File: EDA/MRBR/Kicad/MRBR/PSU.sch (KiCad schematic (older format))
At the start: 3 parts, among them U2 NCP1117ST33T3G

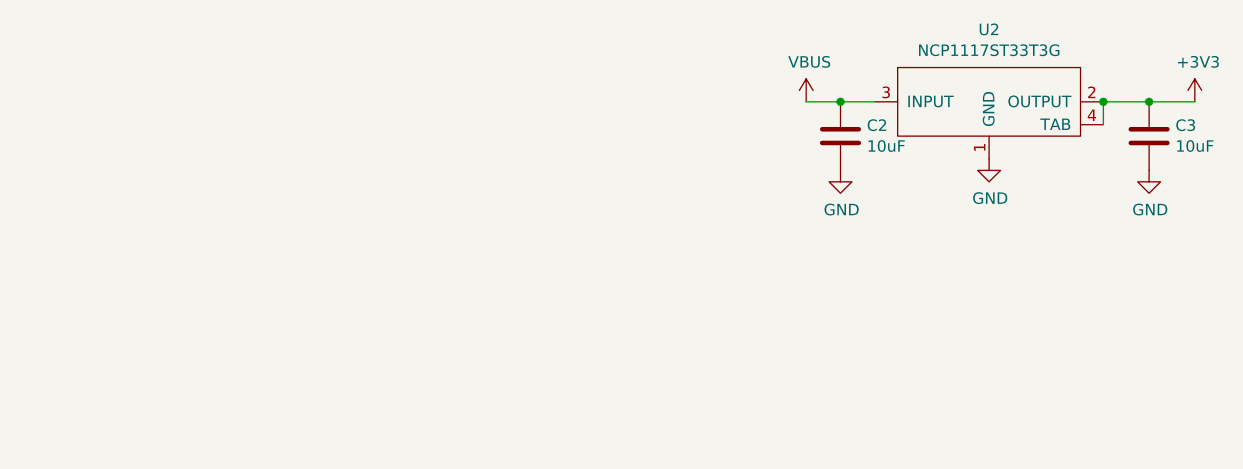
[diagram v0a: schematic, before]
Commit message: Added barrel jack to PSU
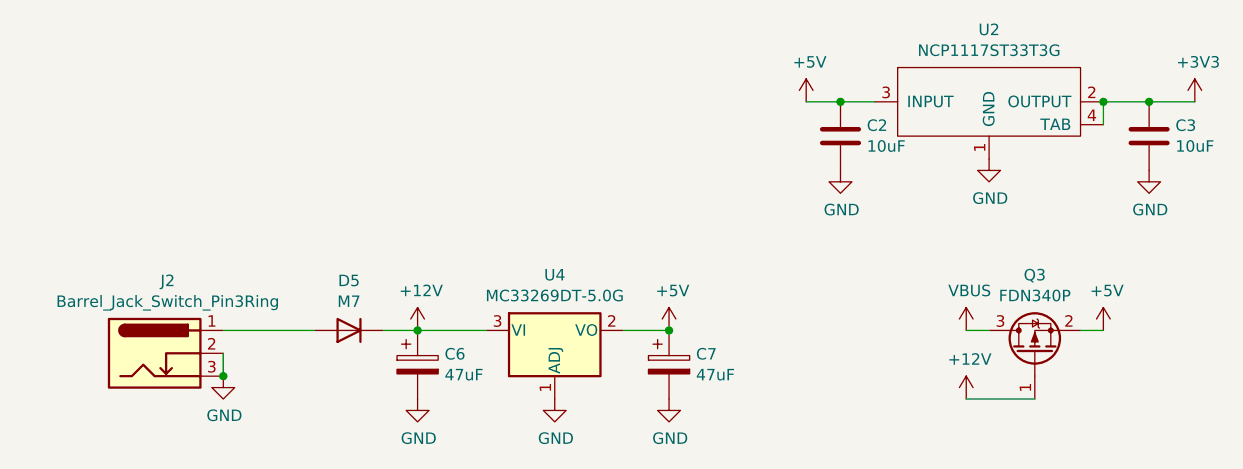
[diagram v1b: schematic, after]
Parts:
- added C6, C7: 47uF, Capacitor_SMD:CP_Elec_6.3x7.7, symbol Device:CP
- added D5: M7, Diode_SMD:D_SMA, symbol Device:D
- added J2: Barrel_Jack_Switch_Pin3Ring, Connector_BarrelJack:BarrelJack_Wuerth_6941xx301002, symbol Connector:Barrel_Jack_Switch_Pin3Ring
- added Q3: FDN340P, Package_TO_SOT_SMD:SOT-23, symbol Transistor_FET:FDN340P
- added U4: MC33269DT-5.0G, Package_TO_SOT_SMD:TO-252-2, symbol Regulator_Linear:MC33269DT-5.0G
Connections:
- net GND: now also C6.2, C7.2, J2.2, J2.3, U4.1 (ADJ)
- net VBUS: now also Q3.3 (D); no longer C2.1, U2.3 (INPUT)
- new net: D5.2 (A), J2.1
- new net +12V: C6.1, D5.1 (K), Q3.1 (G), U4.3 (VI)
- new net +5V: C2.1, C7.1, Q3.2 (S), U2.3 (INPUT), U4.2 (VO)
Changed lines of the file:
@@
-$EndComp
-$Comp
-L power:VBUS #PWR06
-U 1 1 611D0F4B
-P 4750 2750
-F 0 "#PWR06" H 4750 2600 50  0001 C CNN
-F 1 "VBUS" H 4765 2923 50  0000 C CNN
-F 2 "" H 4750 2750 50  0001 C CNN
-F 3 "" H 4750 2750 50  0001 C CNN
-	1    4750 2750
-	1    0    0    -1
 $EndComp
 $Comp
@@
 Wire Wire Line
 	6250 2750 6450 2750
+$Comp
+L Connector:Barrel_Jack_Switch_Pin3Ring J2
+U 1 1 612526B4
+P 1900 3850
+F 0 "J2" H 1957 4167 50  0000 C CNN
+F 1 "Barrel_Jack_Switch_Pin3Ring" H 1957 4076 50  0000 C CNN
+F 2 "Connector_BarrelJack:BarrelJack_Wuerth_6941xx301002" H 1950 3810 50  0001 C CNN
+F 3 "~" H 1950 3810 50  0001 C CNN
+	1    1900 3850
+	1    0    0    -1
+$EndComp
+$Comp
+L Device:D D5
+U 1 1 612543C2
+P 2750 3750
+F 0 "D5" H 2750 3533 50  0000 C CNN
+F 1 "M7" H 2750 3624 50  0000 C CNN
+F 2 "Diode_SMD:D_SMA" H 2750 3750 50  0001 C CNN
+F 3 "~" H 2750 3750 50  0001 C CNN
+	1    2750 3750
+	-1   0    0    1
+$EndComp
+Wire Wire Line
+	2200 3750 2600 3750
+Wire Wire Line
+	2200 3850 2200 3950
+$Comp
+L power:GND #PWR020
+U 1 1 612552FD
+P 2200 3950
+F 0 "#PWR020" H 2200 3700 50  0001 C CNN
+F 1 "GND" H 2205 3777 50  0000 C CNN
+F 2 "" H 2200 3950 50  0001 C CNN
+F 3 "" H 2200 3950 50  0001 C CNN
+	1    2200 3950
+	1    0    0    -1
+$EndComp
+Connection ~ 2200 3950
+$Comp
+L Device:CP C6
+U 1 1 61255DE4
+P 3050 3900
+F 0 "C6" H 3168 3946 50  0000 L CNN
+F 1 "47uF" H 3168 3855 50  0000 L CNN
+F 2 "Capacitor_SMD:CP_Elec_6.3x7.7" H 3088 3750 50  0001 C CNN
+F 3 "~" H 3050 3900 50  0001 C CNN
+	1    3050 3900
+	1    0    0    -1
+$EndComp
+$Comp
+L Device:CP C7
+U 1 1 61257275
+P 4150 3900
+F 0 "C7" H 4268 3946 50  0000 L CNN
+F 1 "47uF" H 4268 3855 50  0000 L CNN
+F 2 "Capacitor_SMD:CP_Elec_6.3x7.7" H 4188 3750 50  0001 C CNN
+F 3 "~" H 4150 3900 50  0001 C CNN
+	1    4150 3900
+	1    0    0    -1
+$EndComp
+$Comp
+L Regulator_Linear:MC33269DT-5.0G U4
+U 1 1 6125C1E8
+P 3650 3750
+F 0 "U4" H 3650 3992 50  0000 C CNN
+F 1 "MC33269DT-5.0G" H 3650 3901 50  0000 C CNN
+F 2 "Package_TO_SOT_SMD:TO-252-2" H 3650 4000 50  0001 C CIN
+F 3 "https://datasheet.lcsc.com/lcsc/1811141628_ON-Semiconductor-MC33269DT-5-0G_C232420.pdf" H 3650 3750 50  0001 C CNN
+	1    3650 3750
+	1    0    0    -1
+$EndComp
+Wire Wire Line
+	2900 3750 3050 3750
+Connection ~ 3050 3750
+Wire Wire Line
+	3050 3750 3350 3750
+$Comp
+L power:GND #PWR024
+U 1 1 6125CEDD
+P 3050 4050
+F 0 "#PWR024" H 3050 3800 50  0001 C CNN
+F 1 "GND" H 3055 3877 50  0000 C CNN
+F 2 "" H 3050 4050 50  0001 C CNN
+F 3 "" H 3050 4050 50  0001 C CNN
+	1    3050 4050
+	1    0    0    -1
+$EndComp
+$Comp
+L power:GND #PWR025
+U 1 1 6125D4AB
+P 3650 4050
+F 0 "#PWR025" H 3650 3800 50  0001 C CNN
+F 1 "GND" H 3655 3877 50  0000 C CNN
+F 2 "" H 3650 4050 50  0001 C CNN
+F 3 "" H 3650 4050 50  0001 C CNN
+	1    3650 4050
+	1    0    0    -1
+$EndComp
+$Comp
+L power:GND #PWR027
+U 1 1 6125D868
+P 4150 4050
+F 0 "#PWR027" H 4150 3800 50  0001 C CNN
+F 1 "GND" H 4155 3877 50  0000 C CNN
+F 2 "" H 4150 4050 50  0001 C CNN
+F 3 "" H 4150 4050 50  0001 C CNN
+	1    4150 4050
+	1    0    0    -1
+$EndComp
+Wire Wire Line
+	3950 3750 4150 3750
+$Comp
+L power:+12V #PWR023
+U 1 1 6125E8E0
+P 3050 3750
+F 0 "#PWR023" H 3050 3600 50  0001 C CNN
+F 1 "+12V" H 3065 3923 50  0000 C CNN
+F 2 "" H 3050 3750 50  0001 C CNN
+F 3 "" H 3050 3750 50  0001 C CNN
+	1    3050 3750
+	1    0    0    -1
+$EndComp
+$Comp
+L power:+5V #PWR026
+U 1 1 61262881
+P 4150 3750
+F 0 "#PWR026" H 4150 3600 50  0001 C CNN
+F 1 "+5V" H 4165 3923 50  0000 C CNN
+F 2 "" H 4150 3750 50  0001 C CNN
+F 3 "" H 4150 3750 50  0001 C CNN
+	1    4150 3750
+	1    0    0    -1
+$EndComp
+Connection ~ 4150 3750
+$Comp
+L Transistor_FET:FDN340P Q3
+U 1 1 61266027
+P 5750 3850
+F 0 "Q3" V 6092 3850 50  0000 C CNN
+F 1 "FDN340P" V 6001 3850 50  0000 C CNN
+F 2 "Package_TO_SOT_SMD:SOT-23" H 5950 3775 50  0001 L CIN
+F 3 "http://www.vishay.com/docs/70209/70209.pdf" H 5750 3850 50  0001 L CNN
+	1    5750 3850
+	0    -1   -1   0
+$EndComp
+$Comp
+L power:VBUS #PWR029
+U 1 1 612695EC
+P 5450 3750
+F 0 "#PWR029" H 5450 3600 50  0001 C CNN
+F 1 "VBUS" H 5465 3923 50  0000 C CNN
+F 2 "" H 5450 3750 50  0001 C CNN
+F 3 "" H 5450 3750 50  0001 C CNN
+	1    5450 3750
+	1    0    0    -1
+$EndComp
+Wire Wire Line
+	5450 3750 5550 3750
+Wire Wire Line
+	5450 4050 5750 4050
+Wire Wire Line
+	5950 3750 6050 3750
+$Comp
+L power:+5V #PWR031
+U 1 1 6126DB49
+P 6050 3750
+F 0 "#PWR031" H 6050 3600 50  0001 C CNN
+F 1 "+5V" H 6065 3923 50  0000 C CNN
+F 2 "" H 6050 3750 50  0001 C CNN
+F 3 "" H 6050 3750 50  0001 C CNN
+	1    6050 3750
+	1    0    0    -1
+$EndComp
+$Comp
+L power:+12V #PWR030
+U 1 1 6126E27A
+P 5450 4050
+F 0 "#PWR030" H 5450 3900 50  0001 C CNN
+F 1 "+12V" H 5465 4223 50  0000 C CNN
+F 2 "" H 5450 4050 50  0001 C CNN
+F 3 "" H 5450 4050 50  0001 C CNN
+	1    5450 4050
+	1    0    0    -1
+$EndComp
+$Comp
+L power:+5V #PWR028
+U 1 1 6126EBDF
+P 4750 2750
+F 0 "#PWR028" H 4750 2600 50  0001 C CNN
+F 1 "+5V" H 4765 2923 50  0000 C CNN
+F 2 "" H 4750 2750 50  0001 C CNN
+F 3 "" H 4750 2750 50  0001 C CNN
+	1    4750 2750
+	1    0    0    -1
+$EndComp
 $EndSCHEMATC
